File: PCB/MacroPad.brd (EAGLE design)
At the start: 76.2 x 76.2 mm, 42 parts, among them SW00 SWITCH-SMD-EVQP-P2602W, SW01 KEYSWITCH-PLAIN-MX-1U, SW02 KEYSWITCH-PLAIN-MX-1U, SW03 KEYSWITCH-PLAIN-MX-1U, SW04 KEYSWITCH-PLAIN-MX-1U, SW05 KEYSWITCH-PLAIN-MX-1U, SW06 KEYSWITCH-PLAIN-MX-1U, SW07 KEYSWITCH-PLAIN-MX-1U, SW08 KEYSWITCH-PLAIN-MX-1U, SW09 KEYSWITCH-PLAIN-MX-1U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

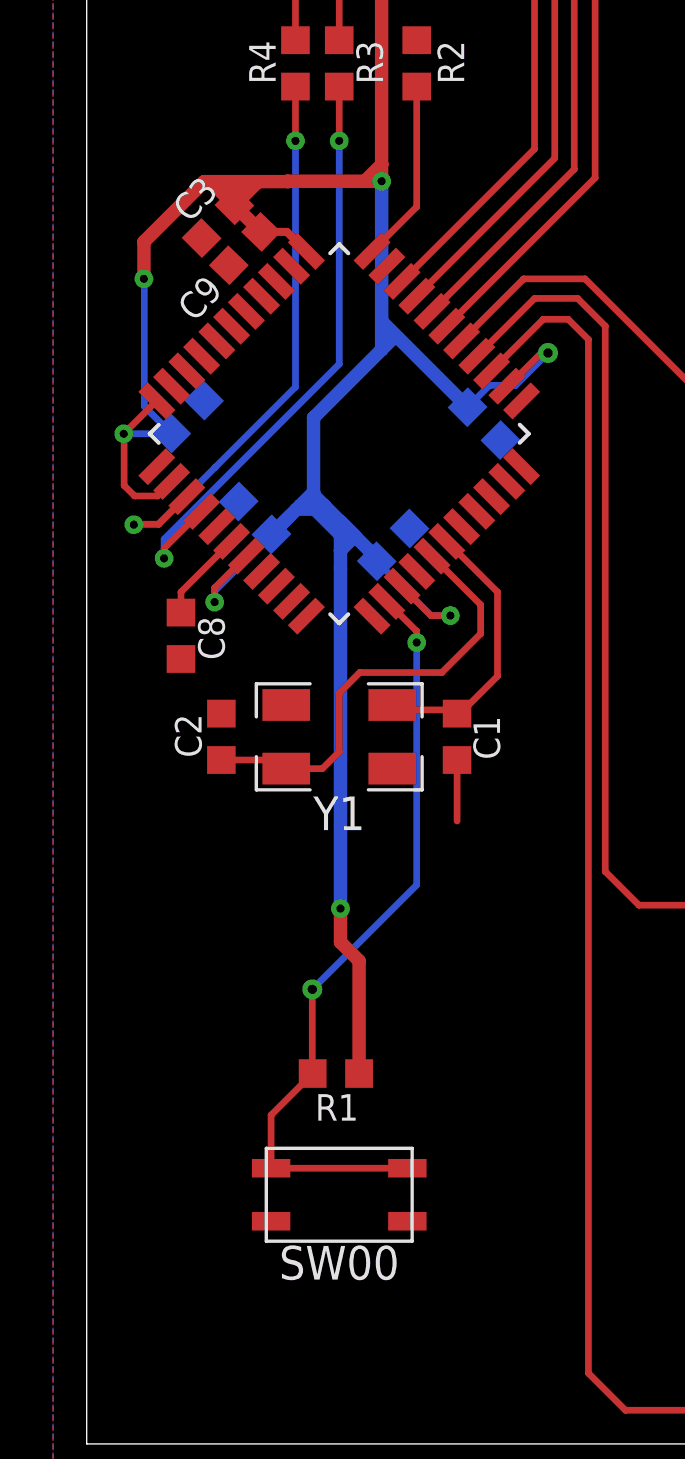
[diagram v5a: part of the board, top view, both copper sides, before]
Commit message: Rename components based on board position
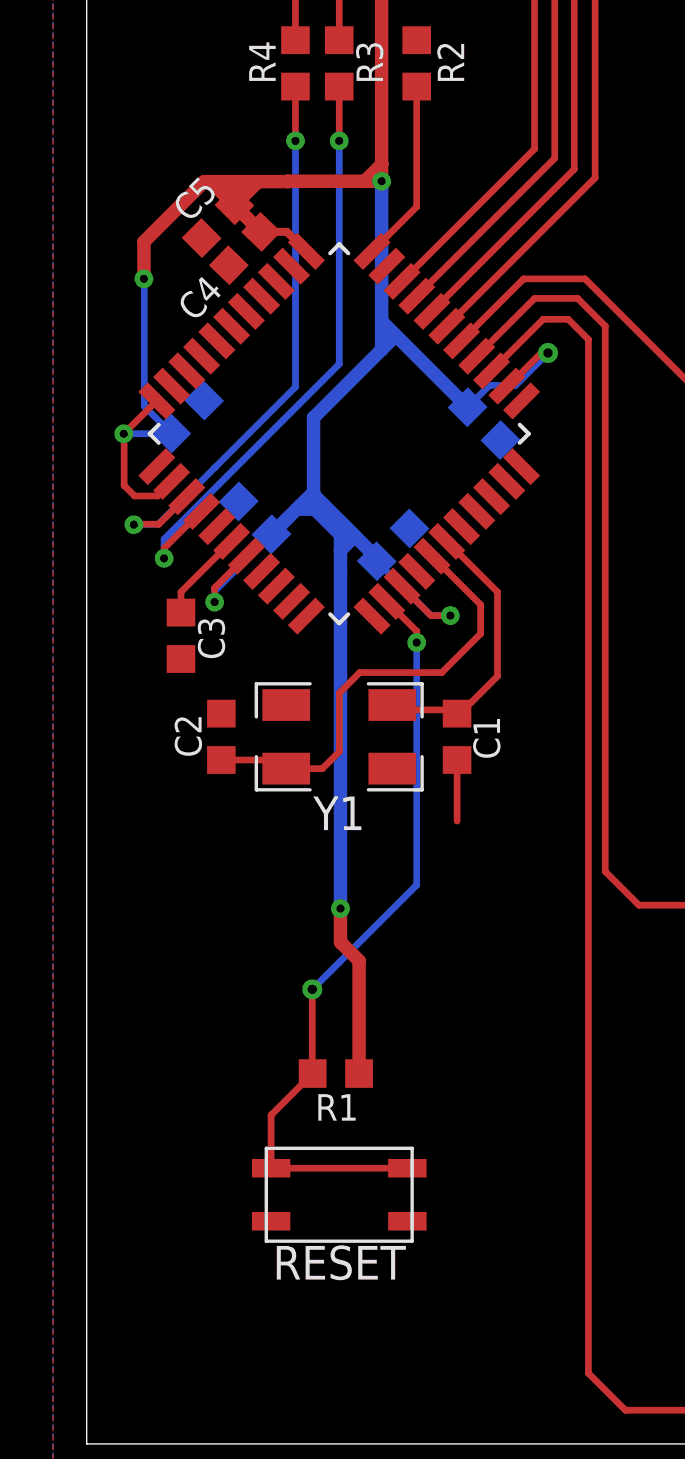
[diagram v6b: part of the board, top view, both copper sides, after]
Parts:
- C3: value 4.7u -> 1u
- C5: value 0.1u -> 4.7u
- C8: value 1u -> 0.1u
- moved C3 15.7 mm to (3.56, 30.5), turned to 270 degrees
- moved C4 10.2 mm to (5.97, 45.1), flipped to the top, turned to 226 degrees
- moved C5 7.45 mm to (4.95, 46.1), flipped to the top, turned to 225 degrees
- moved C9 6.71 mm to (3.81, 38.7), flipped to the bottom, turned to 135 degrees
- moved C6 5.72 mm to (15.0, 38.5), turned to 225 degrees
- moved C7 5.72 mm to (11.6, 33.9), turned to 135 degrees
- moved C8 5.25 mm to (6.35, 34.9), flipped to the bottom, turned to 45 degrees
- renumbered SW00 to RESET
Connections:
- net UCAP: now also C3.1; no longer C8.1
- net VCC: now also C8.1; no longer C3.1
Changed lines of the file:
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@@
 <attribute name="OC_NEWARK" value="96M1143" x="5.08" y="26.67" size="1.778" layer="27" rot="R270" display="off"/>
 </element>
-<element name="C3" library="Components" package="C0603" value="4.7u" x="4.953" y="46.101" smashed="yes" rot="R225">
+<element name="C5" library="Components" package="C0603" value="4.7u" x="4.953" y="46.101" smashed="yes" rot="R225">
 <attribute name="MF" value="" x="4.953" y="46.101" size="1.778" layer="27" rot="R225" display="off"/>
 <attribute name="MPN" value="" x="4.953" y="46.101" size="1.778" layer="27" rot="R225" display="off"/>
@@
 <attribute name="OC_NEWARK" value="unknown" x="4.953" y="46.101" size="1.778" layer="27" rot="R225" display="off"/>
 </element>
-<element name="C4" library="Components" package="C0603" value="0.1u" x="6.35" y="34.925" smashed="yes" rot="MR45">
+<element name="C8" library="Components" package="C0603" value="0.1u" x="6.35" y="34.925" smashed="yes" rot="MR45">
 <attribute name="MF" value="" x="6.35" y="34.925" size="1.778" layer="28" rot="MR45" display="off"/>
 <attribute name="MPN" value="" x="6.35" y="34.925" size="1.778" layer="28" rot="MR45" display="off"/>
@@
 <attribute name="OC_NEWARK" value="unknown" x="6.35" y="34.925" size="1.778" layer="28" rot="MR45" display="off"/>
 </element>
-<element name="C5" library="Components" package="C0603" value="0.1u" x="3.81" y="38.735" smashed="yes" rot="MR135">
+<element name="C9" library="Components" package="C0603" value="0.1u" x="3.81" y="38.735" smashed="yes" rot="MR135">
 <attribute name="MF" value="" x="3.81" y="38.735" size="1.778" layer="28" rot="MR135" display="off"/>
 <attribute name="MPN" value="" x="3.81" y="38.735" size="1.778" layer="28" rot="MR135" display="off"/>
@@
 <attribute name="OC_NEWARK" value="unknown" x="3.81" y="38.735" size="1.778" layer="28" rot="MR135" display="off"/>
 </element>
-<element name="C6" library="Components" package="C0603" value="0.1u" x="11.557" y="33.909" smashed="yes" rot="MR135">
+<element name="C7" library="Components" package="C0603" value="0.1u" x="11.557" y="33.909" smashed="yes" rot="MR135">
 <attribute name="MF" value="" x="11.557" y="33.909" size="1.778" layer="28" rot="MR135" display="off"/>
 <attribute name="MPN" value="" x="11.557" y="33.909" size="1.778" layer="28" rot="MR135" display="off"/>
@@
 <attribute name="OC_NEWARK" value="unknown" x="11.557" y="33.909" size="1.778" layer="28" rot="MR135" display="off"/>
 </element>
-<element name="C7" library="Components" package="C0603" value="0.1u" x="14.986" y="38.481" smashed="yes" rot="MR225">
+<element name="C6" library="Components" package="C0603" value="0.1u" x="14.986" y="38.481" smashed="yes" rot="MR225">
 <attribute name="MF" value="" x="14.986" y="38.481" size="1.778" layer="28" rot="MR225" display="off"/>
 <attribute name="MPN" value="" x="14.986" y="38.481" size="1.778" layer="28" rot="MR225" display="off"/>
@@
 <attribute name="OC_NEWARK" value="unknown" x="14.986" y="38.481" size="1.778" layer="28" rot="MR225" display="off"/>
 </element>
-<element name="C8" library="Components" package="C0603" value="1u" x="3.556" y="30.48" smashed="yes" rot="R270">
+<element name="C3" library="Components" package="C0603" value="1u" x="3.556" y="30.48" smashed="yes" rot="R270">
 <attribute name="MF" value="" x="3.556" y="30.48" size="1.778" layer="27" rot="R270" display="off"/>
 <attribute name="MPN" value="" x="3.556" y="30.48" size="1.778" layer="27" rot="R270" display="off"/>
@@
 <attribute name="OC_NEWARK" value="unknown" x="7.874" y="52.07" size="1.778" layer="27" rot="R270" display="off"/>
 </element>
-<element name="SW00" library="Hardware" package="SWITCH-SMD-EVQP-P2602W" value="SWITCH-SMD-EVQP-P2602W" x="9.525" y="9.398" smashed="yes">
+<element name="RESET" library="Hardware" package="SWITCH-SMD-EVQP-P2602W" value="SWITCH-SMD-EVQP-P2602W" x="9.525" y="9.398" smashed="yes">
 <attribute name="MF" value="" x="9.525" y="9.398" size="1.778" layer="27" display="off"/>
 <attribute name="MPN" value="" x="9.525" y="9.398" size="1.778" layer="27" display="off"/>
@@
 <attribute name="VALUE" x="3.81" y="74.93" size="1.27" layer="27" rot="R270"/>
 </element>
-<element name="C9" library="Components" package="C0603" value="0.1u" x="5.969" y="45.085" smashed="yes" rot="R226">
+<element name="C4" library="Components" package="C0603" value="0.1u" x="5.969" y="45.085" smashed="yes" rot="R226">
 <attribute name="MF" value="" x="5.969" y="45.085" size="1.778" layer="27" rot="R226" display="off"/>
 <attribute name="MPN" value="" x="5.969" y="45.085" size="1.778" layer="27" rot="R226" display="off"/>
@@
 </signal>
 <signal name="VCC">
-<contactref element="C3" pad="1"/>
-<contactref element="C4" pad="1"/>
 <contactref element="C5" pad="1"/>
+<contactref element="C8" pad="1"/>
+<contactref element="C9" pad="1"/>
+<contactref element="C7" pad="1"/>
 <contactref element="C6" pad="1"/>
-<contactref element="C7" pad="1"/>
 <contactref element="R1" pad="1"/>
 <contactref element="USB1" pad="VCC"/>
@@
 <wire x1="2.175284375" y1="39.13228125" x2="3.191284375" y2="38.11628125" width="0.254" layer="16"/>
 <wire x1="11.125" y1="48.26" x2="11.125" y2="67.55" width="0.508" layer="1"/>
-<contactref element="C9" pad="1"/>
+<contactref element="C4" pad="1"/>
 <wire x1="7.5940625" y1="47.608715625" x2="7.577778125" y2="47.625" width="0.508" layer="1"/>
 <wire x1="6.460715625" y1="47.608715625" x2="5.571715625" y2="46.719715625" width="0.508" layer="1"/>
@@
 </signal>
 <signal name="N$3">
-<contactref element="SW00" pad="2A"/>
-<contactref element="SW00" pad="2B"/>
+<contactref element="RESET" pad="2A"/>
+<contactref element="RESET" pad="2B"/>
 <wire x1="12.095" y1="10.398" x2="6.955" y2="10.398" width="0.254" layer="1"/>
 <wire x1="6.955" y1="10.398" x2="6.955" y2="12.402" width="0.254" layer="1"/>
@@
 </signal>
 <signal name="UCAP">
-<contactref element="C8" pad="1"/>
+<contactref element="C3" pad="1"/>
 <wire x1="3.556" y1="32.131" x2="3.556" y2="31.355" width="0.254" layer="1"/>
 <contactref element="U1" pad="6"/>
@@
 <contactref element="F1" pad="1"/>
 <contactref element="USB1" pad="GND"/>
+<contactref element="C3" pad="2"/>
+<via x="7.874" y="65.151" extent="1-16" drill="0.3048"/>
+<contactref element="C5" pad="2"/>
 <contactref element="C8" pad="2"/>
-<via x="7.874" y="65.151" extent="1-16" drill="0.3048"/>
-<contactref element="C3" pad="2"/>
+<contactref element="C9" pad="2"/>
+<contactref element="C7" pad="2"/>
+<contactref element="C6" pad="2"/>
 <contactref element="C4" pad="2"/>
-<contactref element="C5" pad="2"/>
-<contactref element="C6" pad="2"/>
-<contactref element="C7" pad="2"/>
-<contactref element="C9" pad="2"/>
 <wire x1="12.17571875" y1="34.527715625" x2="12.17571875" y2="34.17928125" width="0.254" layer="16"/>
 <wire x1="4.33428125" y1="45.48228125" x2="4.33428125" y2="45.042165625" width="0.254" layer="1"/>
 <contactref element="C1" pad="1"/>
 <contactref element="C2" pad="1"/>
-<contactref element="SW00" pad="1A"/>
-<contactref element="SW00" pad="1B"/>
+<contactref element="RESET" pad="1A"/>
+<contactref element="RESET" pad="1B"/>
 <contactref element="R2" pad="1"/>
 <wire x1="5.08" y1="27.545" x2="5.13" y2="27.595" width="0.254" layer="1"/>
